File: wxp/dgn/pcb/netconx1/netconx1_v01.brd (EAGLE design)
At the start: 90.2 x 30.2 mm, 2 parts

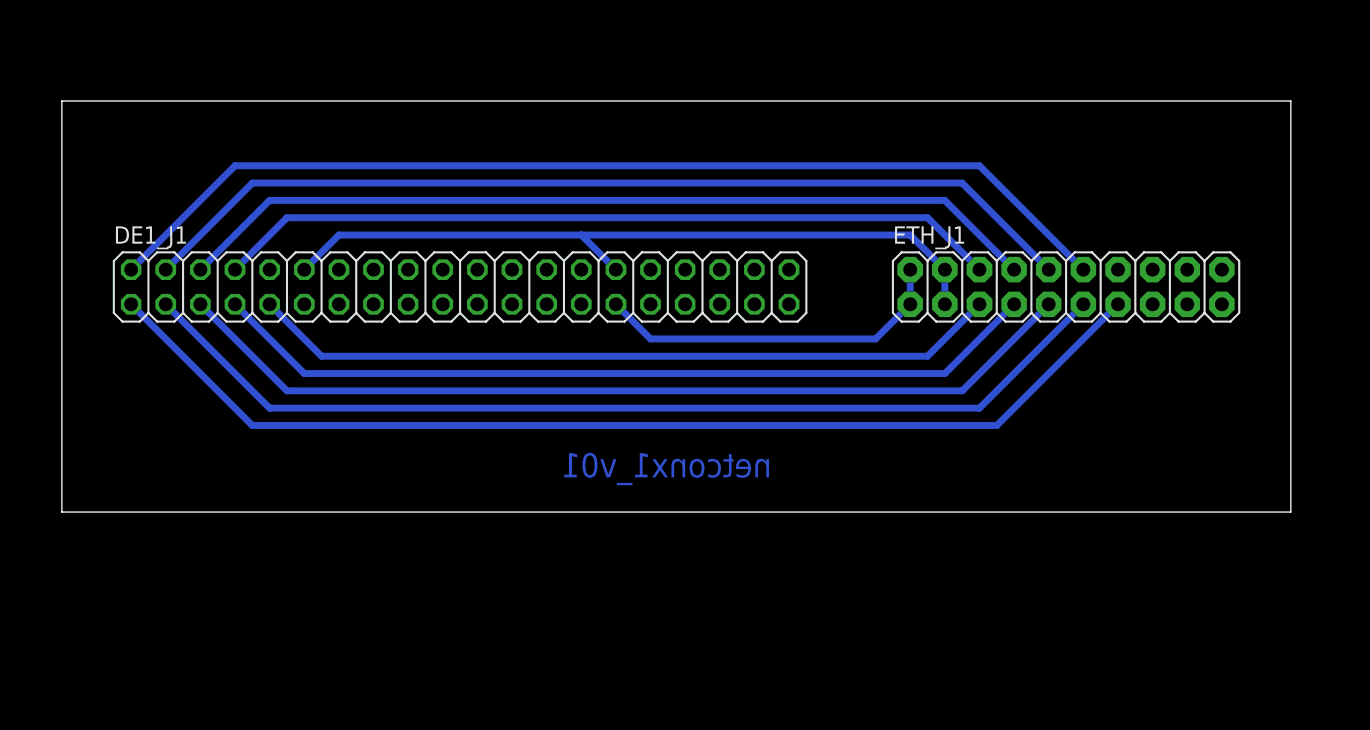
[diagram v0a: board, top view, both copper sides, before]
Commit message: Added ground plane and minor routing changes
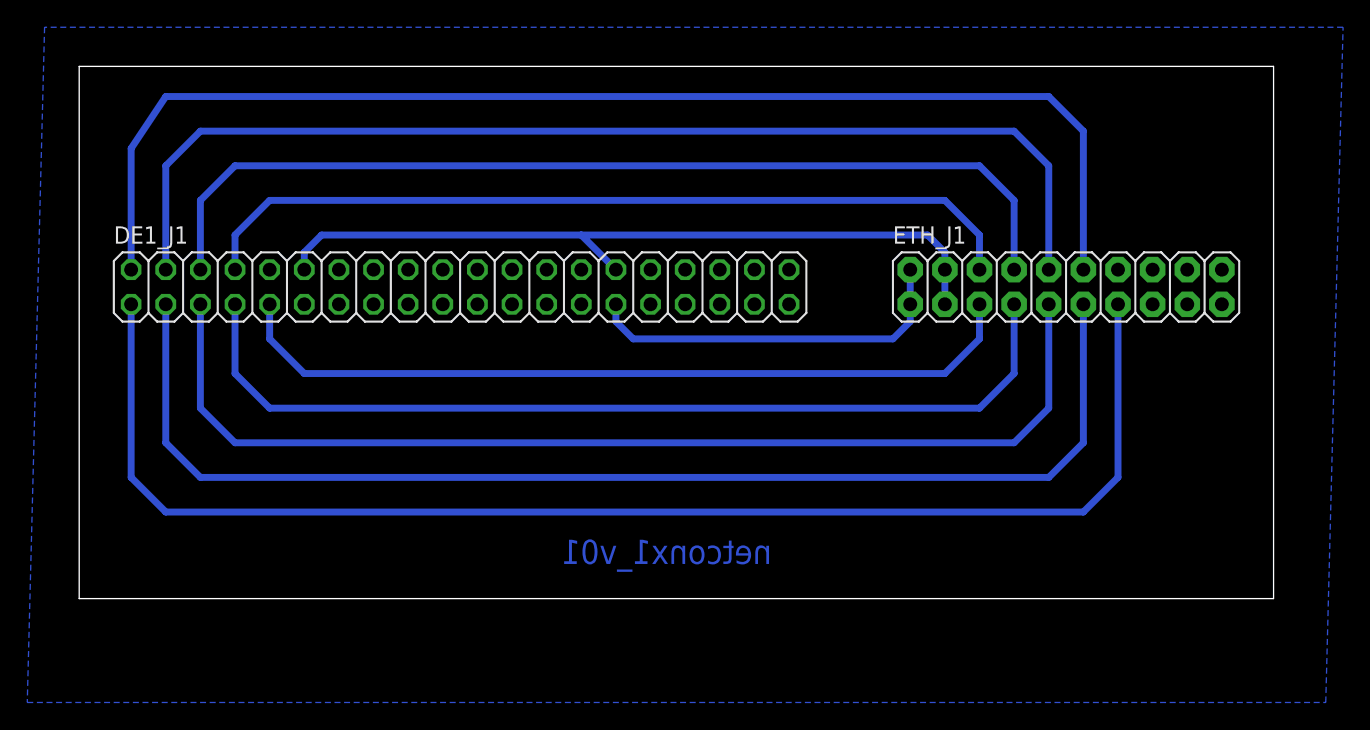
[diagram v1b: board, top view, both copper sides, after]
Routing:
- net N$1: track 79.8 -> 99.9 mm
- net N$2: track 73.6 -> 89.7 mm
- net N$6: track 76.2 -> 92.0 mm
- net N$3: track 67.5 -> 79.6 mm
- net N$7: track 70.0 -> 82.1 mm
- net N$8: track 63.9 -> 72.0 mm
- net N$4: track 61.4 -> 69.4 mm
- net N$9: track 57.8 -> 61.8 mm
- net N$5: track 55.2 -> 59.3 mm
- net GND: track 55.2 -> 56.7 mm
- net VCC: track 26.2 -> 27.7 mm
- added copper zone on layer 16, net GND
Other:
- board size 90.2 x 30.2 mm -> 87.6 x 39 mm
